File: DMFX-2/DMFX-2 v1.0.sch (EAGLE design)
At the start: 55 parts, among them P5 87024-610LF, P7 87024-610LF, SW1X NAVIMEC

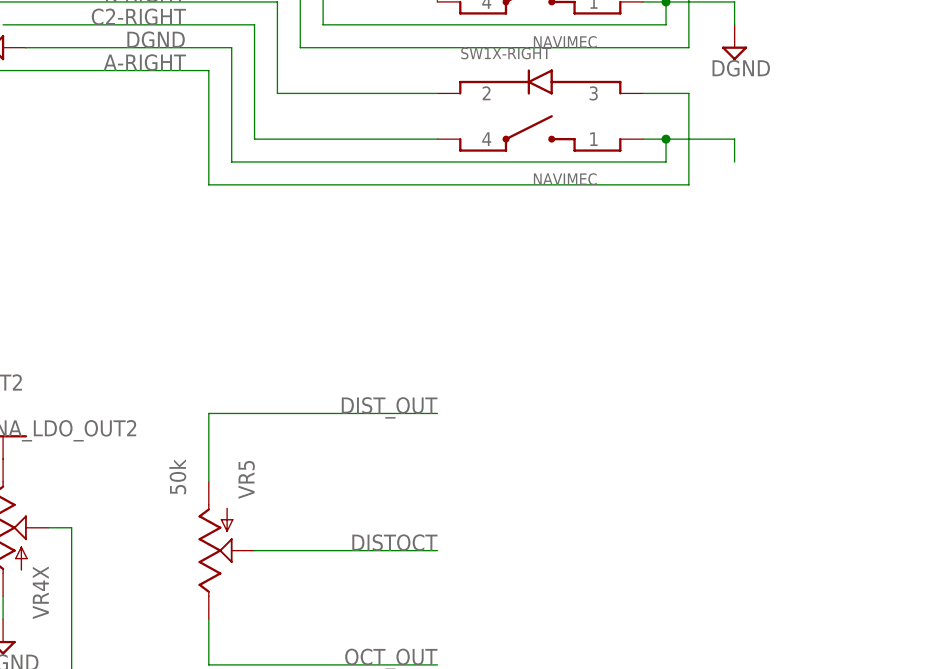
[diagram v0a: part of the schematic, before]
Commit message: 
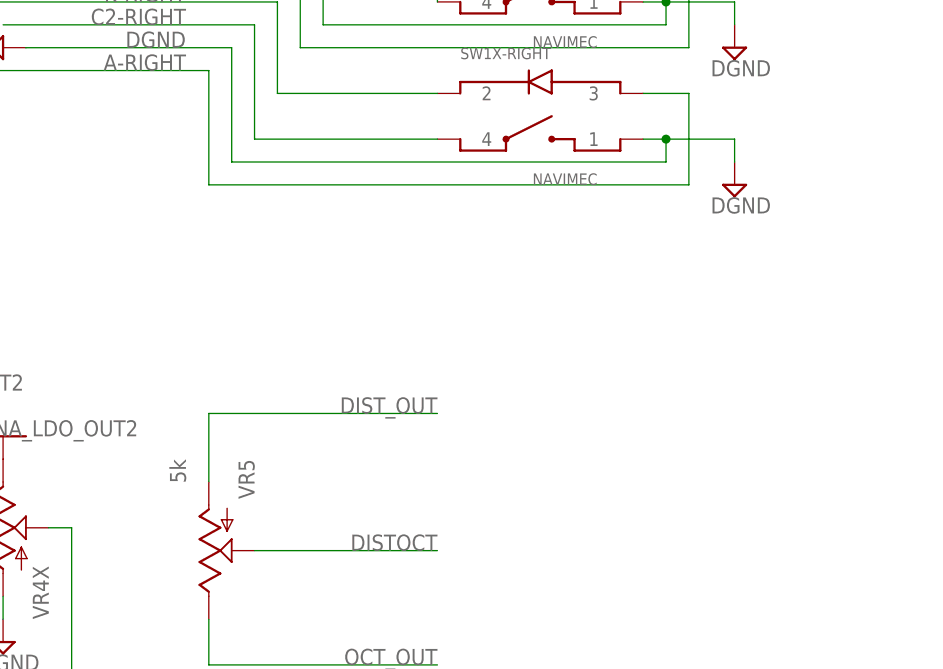
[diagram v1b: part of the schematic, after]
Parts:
- VR5: value 50k -> 5k; MPN EVU-F2AF30B54 -> EVU-F2AF30B53
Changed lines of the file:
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@@
 <grid distance="0.1" unitdist="inch" unit="inch" style="lines" multiple="1" display="no" altdistance="0.01" altunitdist="inch" altunit="inch"/>
 <layers>
-<layer number="1" name="Top" color="4" fill="1" visible="yes" active="no"/>
-<layer number="2" name="Route2" color="1" fill="3" visible="yes" active="no"/>
-<layer number="3" name="Route3" color="4" fill="3" visible="yes" active="no"/>
-<layer number="4" name="Route4" color="1" fill="4" visible="yes" active="no"/>
-<layer number="5" name="Route5" color="4" fill="4" visible="yes" active="no"/>
-<layer number="6" name="Route6" color="1" fill="8" visible="yes" active="no"/>
-<layer number="7" name="Route7" color="4" fill="8" visible="yes" active="no"/>
-<layer number="8" name="Route8" color="1" fill="2" visible="yes" active="no"/>
-<layer number="9" name="Route9" color="4" fill="2" visible="yes" active="no"/>
-<layer number="10" name="Route10" color="1" fill="7" visible="yes" active="no"/>
-<layer number="11" name="Route11" color="4" fill="7" visible="yes" active="no"/>
-<layer number="12" name="Route12" color="1" fill="5" visible="yes" active="no"/>
-<layer number="13" name="Route13" color="4" fill="5" visible="yes" active="no"/>
-<layer number="14" name="Route14" color="1" fill="6" visible="yes" active="no"/>
-<layer number="15" name="Route15" color="4" fill="6" visible="yes" active="no"/>
-<layer number="16" name="Bottom" color="1" fill="1" visible="yes" active="no"/>
-<layer number="17" name="Pads" color="2" fill="1" visible="yes" active="no"/>
-<layer number="18" name="Vias" color="2" fill="1" visible="yes" active="no"/>
-<layer number="19" name="Unrouted" color="6" fill="1" visible="yes" active="no"/>
-<layer number="20" name="Dimension" color="15" fill="1" visible="yes" active="no"/>
-<layer number="21" name="tPlace" color="7" fill="1" visible="yes" active="no"/>
-<layer number="22" name="bPlace" color="7" fill="1" visible="yes" active="no"/>
-<layer number="23" name="tOrigins" color="15" fill="1" visible="yes" active="no"/>
-<layer number="24" name="bOrigins" color="15" fill="1" visible="yes" active="no"/>
-<layer number="25" name="tNames" color="7" fill="1" visible="yes" active="no"/>
-<layer number="26" name="bNames" color="7" fill="1" visible="yes" active="no"/>
-<layer number="27" name="tValues" color="7" fill="1" visible="yes" active="no"/>
-<layer number="28" name="bValues" color="7" fill="1" visible="yes" active="no"/>
+<layer number="1" name="Top" color="4" fill="1" visible="no" active="no"/>
+<layer number="2" name="Route2" color="1" fill="3" visible="no" active="no"/>
+<layer number="3" name="Route3" color="4" fill="3" visible="no" active="no"/>
+<layer number="4" name="Route4" color="1" fill="4" visible="no" active="no"/>
+<layer number="5" name="Route5" color="4" fill="4" visible="no" active="no"/>
+<layer number="6" name="Route6" color="1" fill="8" visible="no" active="no"/>
+<layer number="7" name="Route7" color="4" fill="8" visible="no" active="no"/>
+<layer number="8" name="Route8" color="1" fill="2" visible="no" active="no"/>
+<layer number="9" name="Route9" color="4" fill="2" visible="no" active="no"/>
+<layer number="10" name="Route10" color="1" fill="7" visible="no" active="no"/>
+<layer number="11" name="Route11" color="4" fill="7" visible="no" active="no"/>
+<layer number="12" name="Route12" color="1" fill="5" visible="no" active="no"/>
+<layer number="13" name="Route13" color="4" fill="5" visible="no" active="no"/>
+<layer number="14" name="Route14" color="1" fill="6" visible="no" active="no"/>
+<layer number="15" name="Route15" color="4" fill="6" visible="no" active="no"/>
+<layer number="16" name="Bottom" color="1" fill="1" visible="no" active="no"/>
+<layer number="17" name="Pads" color="2" fill="1" visible="no" active="no"/>
+<layer number="18" name="Vias" color="2" fill="1" visible="no" active="no"/>
+<layer number="19" name="Unrouted" color="6" fill="1" visible="no" active="no"/>
+<layer number="20" name="Dimension" color="15" fill="1" visible="no" active="no"/>
+<layer number="21" name="tPlace" color="7" fill="1" visible="no" active="no"/>
+<layer number="22" name="bPlace" color="7" fill="1" visible="no" active="no"/>
+<layer number="23" name="tOrigins" color="15" fill="1" visible="no" active="no"/>
+<layer number="24" name="bOrigins" color="15" fill="1" visible="no" active="no"/>
+<layer number="25" name="tNames" color="7" fill="1" visible="no" active="no"/>
+<layer number="26" name="bNames" color="7" fill="1" visible="no" active="no"/>
+<layer number="27" name="tValues" color="7" fill="1" visible="no" active="no"/>
+<layer number="28" name="bValues" color="7" fill="1" visible="no" active="no"/>
 <layer number="29" name="tStop" color="7" fill="3" visible="no" active="no"/>
 <layer number="30" name="bStop" color="7" fill="6" visible="no" active="no"/>
@@
 <layer number="35" name="tGlue" color="7" fill="4" visible="no" active="no"/>
 <layer number="36" name="bGlue" color="7" fill="5" visible="no" active="no"/>
-<layer number="37" name="tTest" color="7" fill="1" visible="yes" active="no"/>
-<layer number="38" name="bTest" color="7" fill="1" visible="yes" active="no"/>
+<layer number="37" name="tTest" color="7" fill="1" visible="no" active="no"/>
+<layer number="38" name="bTest" color="7" fill="1" visible="no" active="no"/>
 <layer number="39" name="tKeepout" color="4" fill="11" visible="no" active="no"/>
 <layer number="40" name="bKeepout" color="1" fill="11" visible="no" active="no"/>
@@
 <layer number="44" name="Drills" color="7" fill="1" visible="no" active="no"/>
 <layer number="45" name="Holes" color="7" fill="1" visible="no" active="no"/>
-<layer number="46" name="Milling" color="3" fill="1" visible="yes" active="no"/>
-<layer number="47" name="Measures" color="7" fill="1" visible="yes" active="no"/>
-<layer number="48" name="Document" color="7" fill="1" visible="yes" active="no"/>
-<layer number="49" name="Reference" color="7" fill="1" visible="yes" active="no"/>
-<layer number="50" name="dxf" color="7" fill="1" visible="yes" active="no"/>
-<layer number="51" name="tDocu" color="7" fill="1" visible="yes" active="no"/>
-<layer number="52" name="bDocu" color="7" fill="1" visible="yes" active="no"/>
-<layer number="53" name="tGND_GNDA" color="7" fill="9" visible="yes" active="no"/>
-<layer number="54" name="bGND_GNDA" color="1" fill="9" visible="yes" active="no"/>
-<layer number="56" name="wert" color="7" fill="1" visible="yes" active="no"/>
+<layer number="46" name="Milling" color="3" fill="1" visible="no" active="no"/>
+<layer number="47" name="Measures" color="7" fill="1" visible="no" active="no"/>
+<layer number="48" name="Document" color="7" fill="1" visible="no" active="no"/>
+<layer number="49" name="Reference" color="7" fill="1" visible="no" active="no"/>
+<layer number="50" name="dxf" color="7" fill="1" visible="no" active="no"/>
+<layer number="51" name="tDocu" color="7" fill="1" visible="no" active="no"/>
+<layer number="52" name="bDocu" color="7" fill="1" visible="no" active="no"/>
+<layer number="53" name="tGND_GNDA" color="7" fill="9" visible="no" active="no"/>
+<layer number="54" name="bGND_GNDA" color="1" fill="9" visible="no" active="no"/>
+<layer number="56" name="wert" color="7" fill="1" visible="no" active="no"/>
 <layer number="91" name="Nets" color="2" fill="1" visible="yes" active="yes"/>
 <layer number="92" name="Busses" color="1" fill="1" visible="yes" active="yes"/>
@@
 <attribute name="TP_SIGNAL_NAME" value="K-RIGHT"/>
 </part>
-<part name="VR5" library="SparkFun" deviceset="POT" device="" value="50k">
-<attribute name="MPN" value="EVU-F2AF30B54"/>
-</part>
+<part name="VR5" library="SparkFun" deviceset="POT" device="" value="5k">
+<attribute name="MPN" value="EVU-F2AF30B53"/>
+</part>
+<part name="SUPPLY1" library="supply2" deviceset="DGND" device=""/>
 </parts>
 <sheets>
@@
 <attribute name="MPN" x="154.94" y="129.54" size="1.778" layer="96" display="off"/>
 </instance>
+<instance part="SUPPLY1" gate="G$1" x="213.36" y="170.18"/>
 </instances>
 <busses>
@@
 <junction x="205.74" y="175.26"/>
 <pinref part="SUPPLY216" gate="G$1" pin="DGND"/>
-</segment>
-</net>
+<pinref part="SUPPLY1" gate="G$1" pin="DGND"/>
+</segment>
+</net>
